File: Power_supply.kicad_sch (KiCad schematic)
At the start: 51 parts, among them J1 Transformers, J20 HV_Transformer, J21 LV_Transformer, J22 220V, J23 Transformers, J24 Thyratrone, J25 Anodes_enable, J26 Conn_01x04, J27 Conn_01x04, J28 Conn_01x04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

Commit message: Power supply PCB final 1.0
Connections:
- net GND: now also U4.4
- net at C29.2, Q10.1 (E), R28.2: now also U4.5; no longer U4.1
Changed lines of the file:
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@@
 (kicad_sch (version 20211123) (generator eeschema)
   (paper "A4")
-  (junction (at 118.11 74.93) (diameter 0) (color 0 0 0 0)
-  )
   (junction (at 115.57 104.14) (diameter 0) (color 0 0 0 0)
   )
@@
   (junction (at 233.68 100.33) (diameter 0) (color 0 0 0 0)
   )
+  (junction (at 113.03 74.93) (diameter 0) (color 0 0 0 0)
+  )
   (junction (at 113.03 104.14) (diameter 0) (color 0 0 0 0)
   )
@@
     (stroke (width 0) (type default) (color 0 0 0 0))
   )
-  (wire (pts (xy 97.79 74.93) (xy 118.11 74.93))
+  (wire (pts (xy 97.79 74.93) (xy 113.03 74.93))
     (stroke (width 0) (type default) (color 0 0 0 0))
   )
@@
     (stroke (width 0) (type default) (color 0 0 0 0))
   )
+  (wire (pts (xy 113.03 74.93) (xy 113.03 82.55))
+    (stroke (width 0) (type default) (color 0 0 0 0))
+  )
   (wire (pts (xy 63.5 100.33) (xy 67.31 100.33))
     (stroke (width 0) (type default) (color 0 0 0 0))
@@
     (stroke (width 0) (type default) (color 0 0 0 0))
   )
-  (wire (pts (xy 118.11 74.93) (xy 118.11 82.55))
-    (stroke (width 0) (type default) (color 0 0 0 0))
-  )
   (wire (pts (xy 149.86 148.59) (xy 149.86 142.24))
     (stroke (width 0) (type default) (color 0 0 0 0))
@@
     (stroke (width 0) (type default) (color 0 0 0 0))
   )
+  (wire (pts (xy 115.57 101.6) (xy 115.57 104.14))
+    (stroke (width 0) (type default) (color 0 0 0 0))
+  )
   (wire (pts (xy 76.2 87.63) (xy 76.2 90.17))
     (stroke (width 0) (type default) (color 0 0 0 0))
@@
     (stroke (width 0) (type default) (color 0 0 0 0))
   )
+  (wire (pts (xy 113.03 74.93) (xy 118.11 74.93))
+    (stroke (width 0) (type default) (color 0 0 0 0))
+  )

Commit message: Some errors in the power supply PCB fixed
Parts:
- C1: footprint Capacitor_THT:C_Rect_L7.2mm_W3.0mm_P5.00mm_FKS2_FKP2_MKS2_MKP2 -> spdf1626_lib:C_THT_K73-17_P7.00mm
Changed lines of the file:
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@@
     (property "Reference" "C1" (id 0) (at 134.62 48.26 0))
     (property "Value" "33n" (id 1) (at 134.62 50.8 0))
-    (property "Footprint" "Capacitor_THT:C_Rect_L7.2mm_W3.0mm_P5.00mm_FKS2_FKP2_MKS2_MKP2" (id 2) (at 140.6652 45.72 0)
+    (property "Footprint" "spdf1626_lib:C_THT_K73-17_P7.00mm" (id 2) (at 140.6652 45.72 0)
       (effects (font (size 1.27 1.27)) hide)
     )
@@
     )
     (path "/cac9add8-7e11-41d7-b5dc-f00d79bea5c0"
-      (reference "C1") (unit 1) (value "33n") (footprint "Capacitor_THT:C_Rect_L7.2mm_W3.0mm_P5.00mm_FKS2_FKP2_MKS2_MKP2")
+      (reference "C1") (unit 1) (value "33n") (footprint "spdf1626_lib:C_THT_K73-17_P7.00mm")
     )
     (path "/b4891b91-fcc8-4c2d-a115-d8b03c487b34"

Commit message: New amplifier PCB
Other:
- added sheet Vacuum tube full bridge rectifier (vt_fb_rectifier.kicad_sch)
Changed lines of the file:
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@@
     (pin "1")
+  )
+  (sheet (at 201.93 125.73) (size 35.56 31.75) (fields_autoplaced)
+    (stroke (width 0.1524) (type solid) (color 0 0 0 0))
+    (fill (color 0 0 0 0.0000))
+    (property "Sheet name" "Vacuum tube full bridge rectifier" (id 0) (at 201.93 125.0184 0)
+      (effects (font (size 1.27 1.27)) (justify left bottom))
+    )
+    (property "Sheet file" "vt_fb_rectifier.kicad_sch" (id 1) (at 201.93 158.0646 0)
+      (effects (font (size 1.27 1.27)) (justify left top))
+    )
   )
   (sheet_instances
     (path "/" (page "1"))
+    (path "/58eb1f49-1e5e-4c0c-97da-fb971f13fe25" (page "2"))
   )
   (symbol_instances
+    (path "/58eb1f49-1e5e-4c0c-97da-fb971f13fe25/077354f1-7c81-4092-8cfb-a482b097f5c7"
+      (reference "#PWR01") (unit 1) (value "GND") (footprint "")
+    )
+    (path "/58eb1f49-1e5e-4c0c-97da-fb971f13fe25/bc09f5b8-bc0c-4159-a6f9-b40027ff6da2"
+      (reference "#PWR02") (unit 1) (value "GND") (footprint "")
+    )
+    (path "/58eb1f49-1e5e-4c0c-97da-fb971f13fe25/9dc2ce14-766a-4107-9077-4b8e406cbd7f"
+      (reference "#PWR03") (unit 1) (value "GND") (footprint "")
+    )
     (path "/2fbad06e-061a-4b4a-bc03-c6c3d3c6ed04"
       (reference "#PWR021") (unit 1) (value "+6V") (footprint "")
@@
       (reference "J1") (unit 1) (value "Transformers") (footprint "spdf1626_lib:Connector_1x02_P5mm_Vertical")
     )
+    (path "/58eb1f49-1e5e-4c0c-97da-fb971f13fe25/ed741df9-51b8-4ca6-86fc-56edf0e7ec8b"
+      (reference "J2") (unit 1) (value "IN1") (footprint "Connector_PinHeader_2.54mm:PinHeader_1x01_P2.54mm_Vertical")
+    )
+    (path "/58eb1f49-1e5e-4c0c-97da-fb971f13fe25/a011776d-c403-4b22-9599-3ef343cb1830"
+      (reference "J3") (unit 1) (value "6V") (footprint "spdf1626_lib:PinHeader_1x02_P2.54mm")
+    )
+    (path "/58eb1f49-1e5e-4c0c-97da-fb971f13fe25/4a583b03-7ba0-42d6-ac20-d9bd4ec5453d"
+      (reference "J4") (unit 1) (value "Vout") (footprint "Connector_PinHeader_2.54mm:PinHeader_1x01_P2.54mm_Vertical")
+    )
+    (path "/58eb1f49-1e5e-4c0c-97da-fb971f13fe25/8c6970c9-8528-4787-b893-5feacb6e1304"
+      (reference "J5") (unit 1) (value "IN2") (footprint "Connector_PinHeader_2.54mm:PinHeader_1x01_P2.54mm_Vertical")
+    )
+    (path "/58eb1f49-1e5e-4c0c-97da-fb971f13fe25/4f02c821-edb1-4384-9005-d5946c59583d"
+      (reference "J6") (unit 1) (value "GND") (footprint "Connector_PinHeader_2.54mm:PinHeader_1x01_P2.54mm_Vertical")
+    )
     (path "/460894e8-d679-4399-be51-a7c0384c5016"
       (reference "J20") (unit 1) (value "HV_Transformer") (footprint "spdf1626_lib:PinHeader_1x02_P2.54mm")
@@
       (reference "RV3") (unit 1) (value "10k") (footprint "spdf1626_lib:Potentiometer_THT_CA9V")
     )
+    (path "/58eb1f49-1e5e-4c0c-97da-fb971f13fe25/d0ef9572-f9f1-402b-82aa-afe53ec77b54"
+      (reference "U1") (unit 1) (value "6H2P") (footprint "spdf1626_lib:7-pin_tube_socket")
+    )
+    (path "/58eb1f49-1e5e-4c0c-97da-fb971f13fe25/6e1c18b9-3fea-4204-afc6-38aaff3cd6af"
+      (reference "U2") (unit 1) (value "6H2P") (footprint "spdf1626_lib:7-pin_tube_socket")
+    )
     (path "/57185388-68b8-4c59-8c2f-5b036b0f2170"

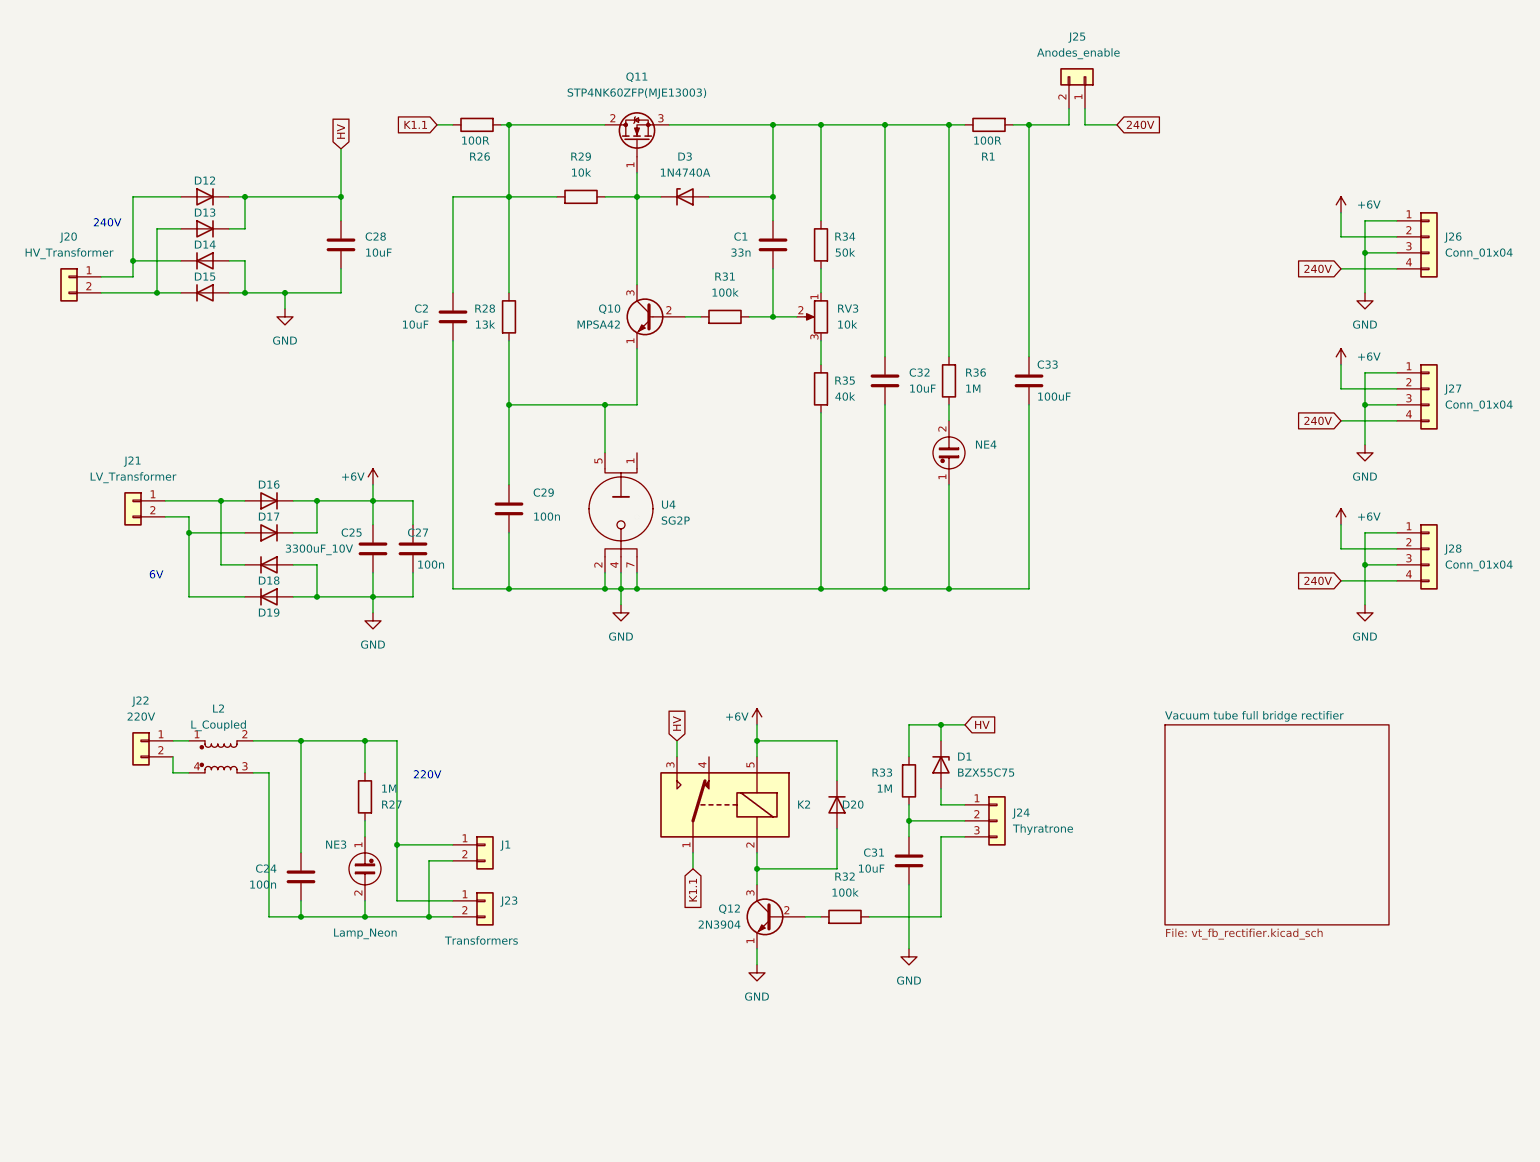
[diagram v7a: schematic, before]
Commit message: Started redesigning power supply
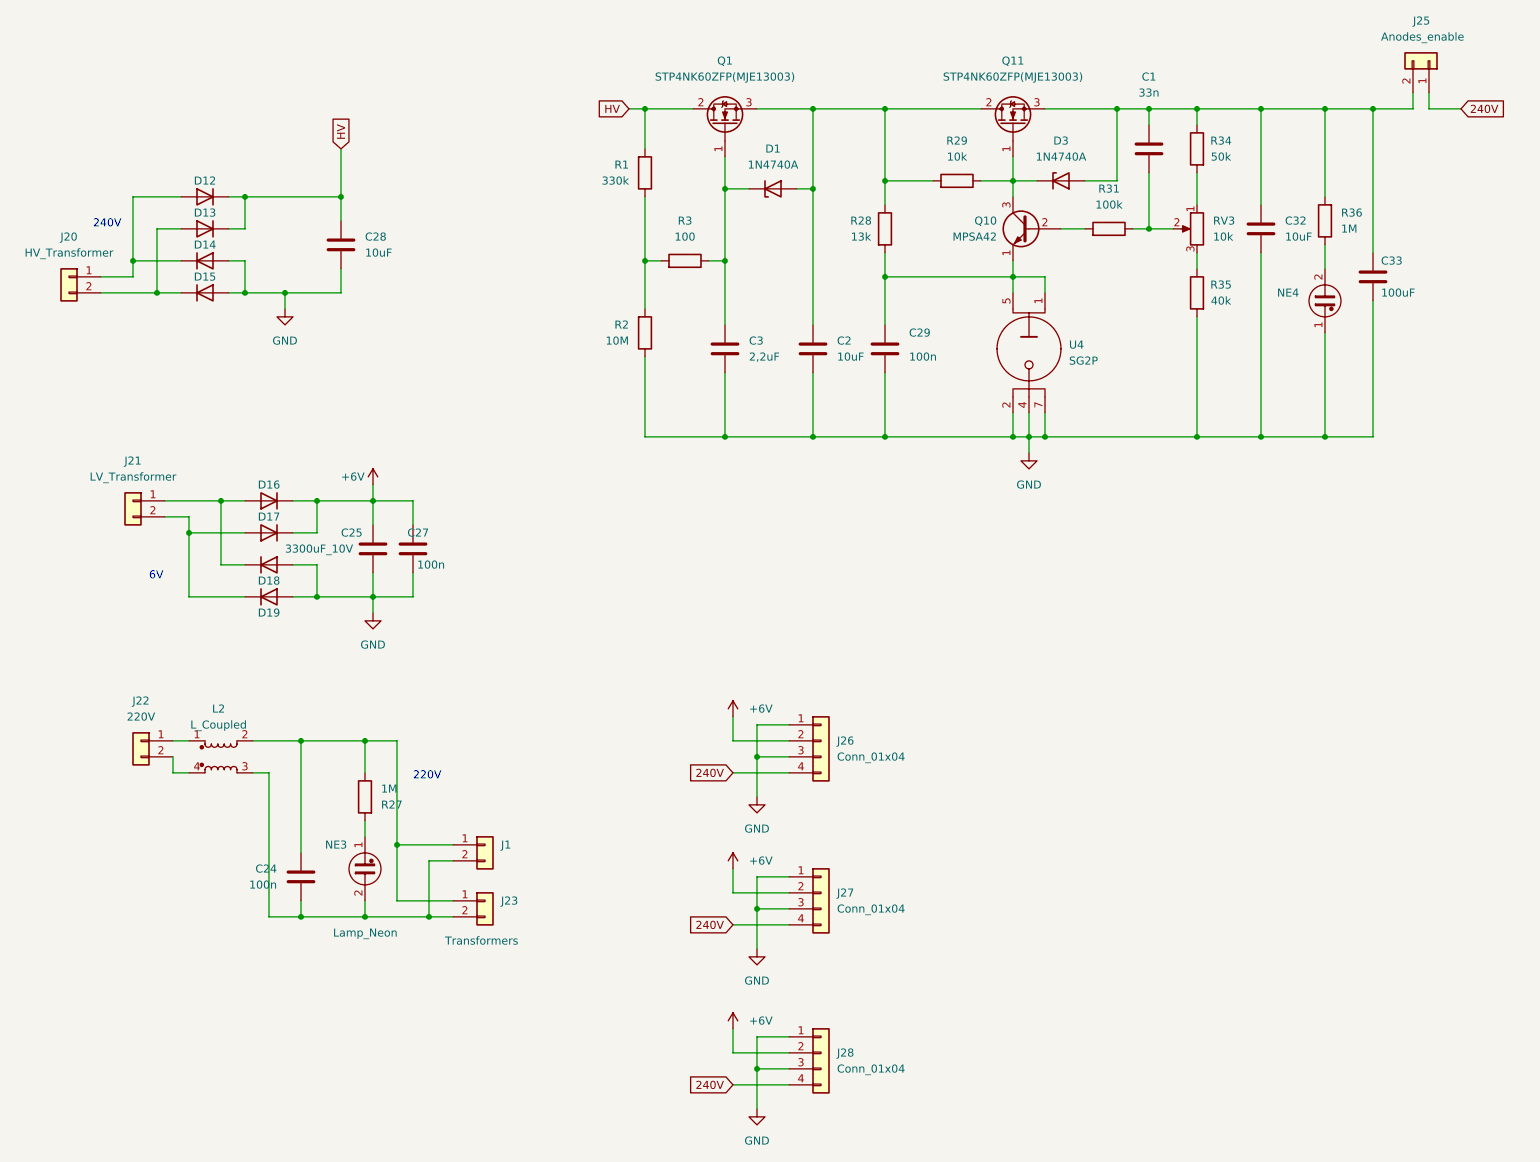
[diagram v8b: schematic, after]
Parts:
- removed C31: 10uF, spdf1626_lib:C_THT_D10.0mm_P5.00mm, symbol Device:C
- removed D20: 1n4007, spdf1626_lib:D_DO-41, symbol Device:D
- removed J24: Thyratrone, spdf1626_lib:PinHeader_1x03_P2.54mm, symbol Connector_Generic:Conn_01x03
- removed K2: SANYOU_SRD_Form_C, Relay_THT:Relay_SPDT_SANYOU_SRD_Series_Form_C, symbol Relay:SANYOU_SRD_Form_C
- removed Q12: 2N3904, Package_TO_SOT_THT:TO-92_Inline, symbol Transistor_BJT:2N3904
- removed R26: 100R, spdf1626_lib:R_THT_1W, symbol Device:R
- removed R32: 100k, spdf1626_lib:R_THT_025W, symbol Device:R
- removed R33: 1M, spdf1626_lib:R_THT_025W, symbol Device:R
- added C3: 2,2uF, spdf1626_lib:C_THT_D10.0mm_P5.00mm, symbol Device:C
- added Q1: STP4NK60ZFP(MJE13003), spdf1626_lib:TO-220-3_Vertical, symbol Transistor_FET:IRF740
- added R2: 10M, spdf1626_lib:R_THT_025W, symbol Device:R
- added R3: 100, spdf1626_lib:R_THT_025W, symbol Device:R
- D1: value BZX55C75 -> 1N4740A; footprint spdf1626_lib:D_THT_DO-35_SOD27_Horizontal -> spdf1626_lib:D_DO-41_short
- D3: footprint spdf1626_lib:D_DO-41 -> spdf1626_lib:D_DO-41_short
- J20, J21: footprint spdf1626_lib:PinHeader_1x02_P2.54mm -> spdf1626_lib:Connector_1x02_P5mm_Vertical
- R1: value 100R -> 330k; footprint spdf1626_lib:R_THT_1W -> spdf1626_lib:R_THT_025W
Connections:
- net GND: now also C3.2, R2.1
- net HV: now also R1.2, Q1.2 (D); no longer D1.1 (K)
- net at C2.1, Q11.2 (D), R28.1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: now also D1.2 (A), Q1.3 (S)
- net at C29.2, Q10.1 (E), R28.2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: now also U4.1
- net at C1.2, C32.1, D3.2 (A)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: now also C33.1, J25.2 (Pin_2); no longer R1.1
- new net: C3.1, D1.1 (K), Q1.1 (G), R3.1
- new net: R1.1, R2.2, R3.2
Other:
- removed sheet Vacuum tube full bridge rectifier
- moved on the sheet: C1, C2, C29, C32, C33, D3, J25, J26, J27, J28, NE4, Q10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
